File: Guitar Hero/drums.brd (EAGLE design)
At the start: 40.6 x 31.1 mm, 10 parts, among them IC1 ICL7641P

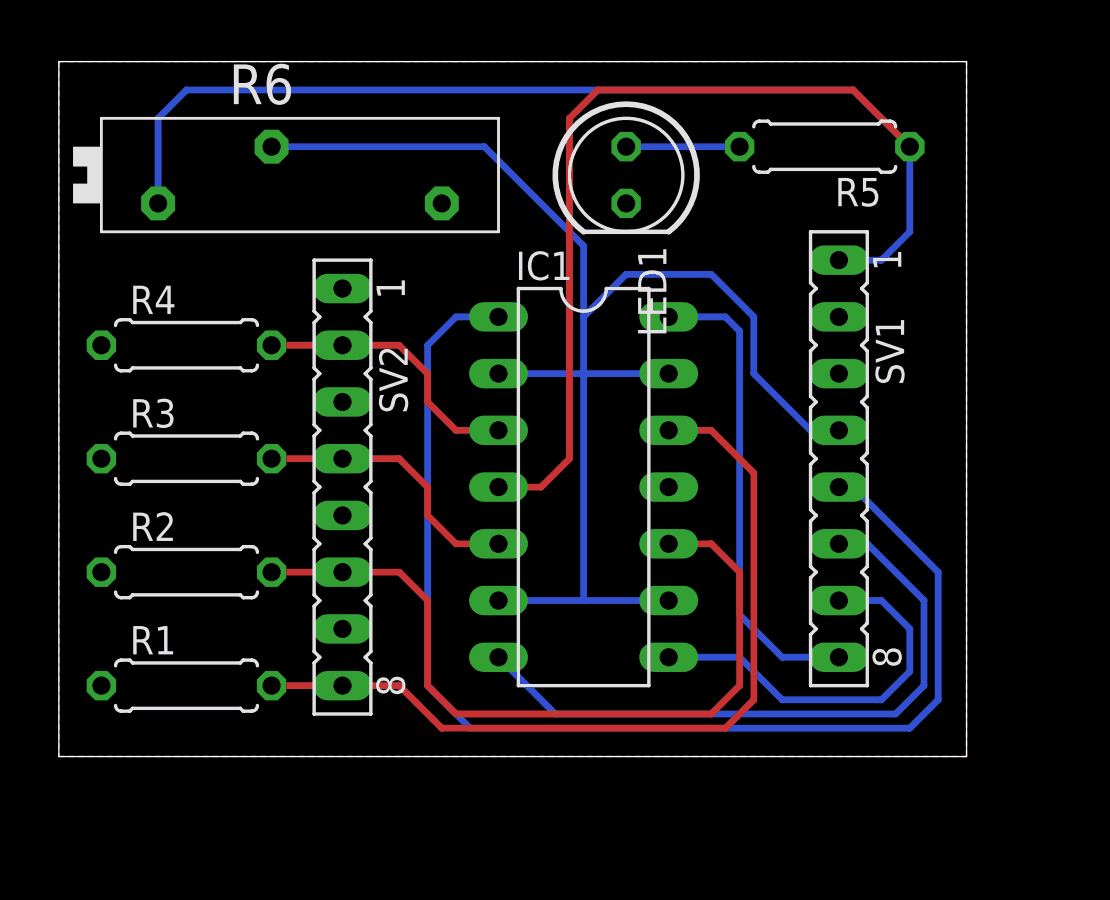
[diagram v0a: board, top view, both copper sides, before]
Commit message: Widened power traces
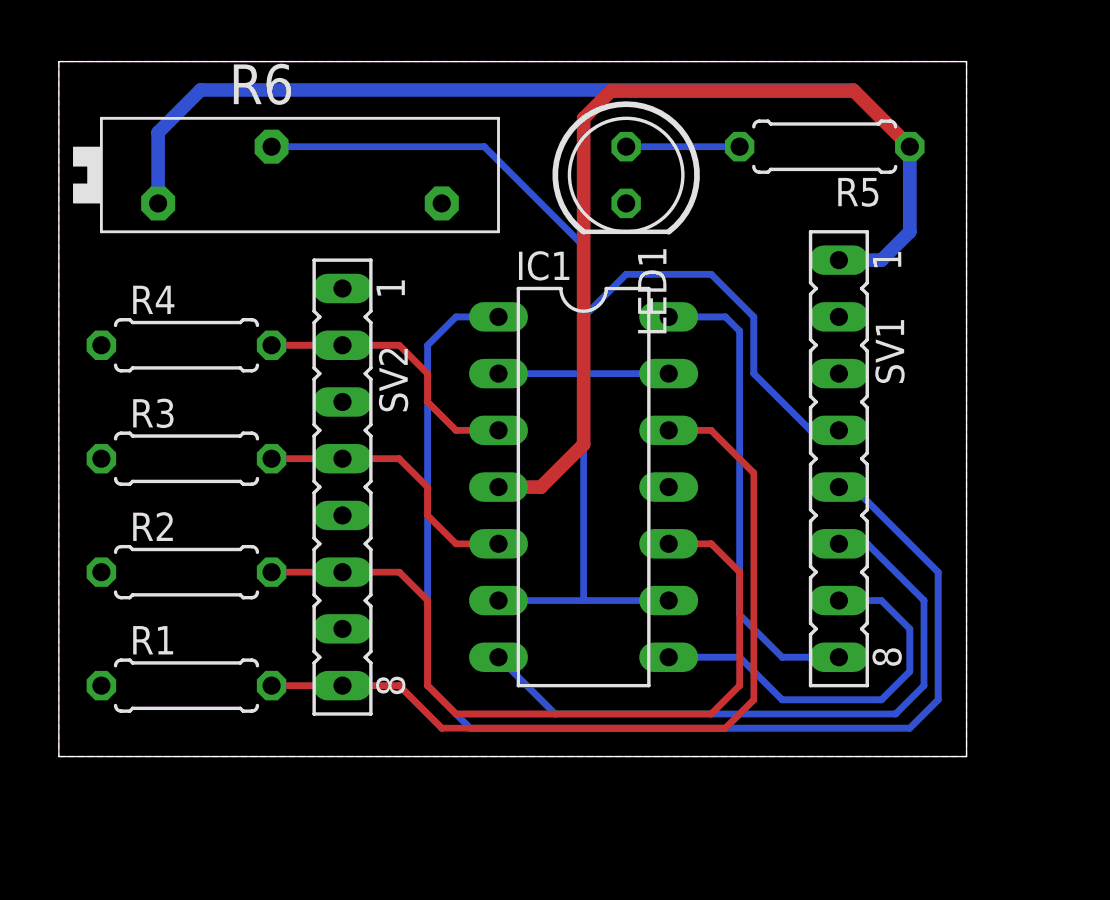
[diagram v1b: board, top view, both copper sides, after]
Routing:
- net VCC: track 82.3 -> 81.5 mm
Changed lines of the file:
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@@
 <contactref element="IC1" pad="4"/>
 <contactref element="R6" pad="1"/>
-<wire x1="48.26" y1="45.72" x2="50.165" y2="45.72" width="0.3048" layer="16"/>
-<wire x1="50.165" y1="45.72" x2="51.435" y2="46.99" width="0.3048" layer="16"/>
-<wire x1="51.435" y1="50.8" x2="51.435" y2="46.99" width="0.3048" layer="16"/>
-<wire x1="17.78" y1="48.26" x2="17.78" y2="52.07" width="0.3048" layer="16"/>
-<wire x1="17.78" y1="52.07" x2="19.05" y2="53.34" width="0.3048" layer="16"/>
-<wire x1="19.05" y1="53.34" x2="48.895" y2="53.34" width="0.3048" layer="16"/>
-<wire x1="48.895" y1="53.34" x2="51.435" y2="50.8" width="0.3048" layer="16"/>
-<wire x1="33.02" y1="35.56" x2="34.925" y2="35.56" width="0.3048" layer="1"/>
-<wire x1="34.925" y1="35.56" x2="36.195" y2="36.83" width="0.3048" layer="1"/>
-<wire x1="36.195" y1="36.83" x2="36.195" y2="52.07" width="0.3048" layer="1"/>
-<wire x1="36.195" y1="52.07" x2="37.465" y2="53.34" width="0.3048" layer="1"/>
-<wire x1="37.465" y1="53.34" x2="48.895" y2="53.34" width="0.3048" layer="1"/>
-<wire x1="48.895" y1="53.34" x2="51.435" y2="50.8" width="0.3048" layer="1"/>
+<wire x1="51.435" y1="50.8" x2="48.9458" y2="53.2892" width="0.6096" layer="1"/>
+<wire x1="48.9458" y1="53.2892" x2="38.0492" y2="53.2892" width="0.6096" layer="1"/>
+<wire x1="38.0492" y1="53.2892" x2="36.83" y2="52.07" width="0.6096" layer="1"/>
+<wire x1="36.83" y1="52.07" x2="36.83" y2="37.465" width="0.6096" layer="1"/>
+<wire x1="36.83" y1="37.465" x2="34.925" y2="35.56" width="0.6096" layer="1"/>
+<wire x1="34.925" y1="35.56" x2="33.02" y2="35.56" width="0.6096" layer="1"/>
+<wire x1="48.26" y1="45.72" x2="50.165" y2="45.72" width="0.6096" layer="16"/>
+<wire x1="50.165" y1="45.72" x2="51.435" y2="46.99" width="0.6096" layer="16"/>
+<wire x1="51.435" y1="46.99" x2="51.435" y2="50.8" width="0.6096" layer="16"/>
+<wire x1="51.435" y1="50.8" x2="48.895" y2="53.34" width="0.6096" layer="16"/>
+<wire x1="48.895" y1="53.34" x2="19.685" y2="53.34" width="0.6096" layer="16"/>
+<wire x1="19.685" y1="53.34" x2="17.78" y2="51.435" width="0.6096" layer="16"/>
+<wire x1="17.78" y1="51.435" x2="17.78" y2="48.26" width="0.6096" layer="16"/>
 </signal>
 <signal name="N$2">

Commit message: Nano++ schematic; guitar hero redo to not use 1/64th bit
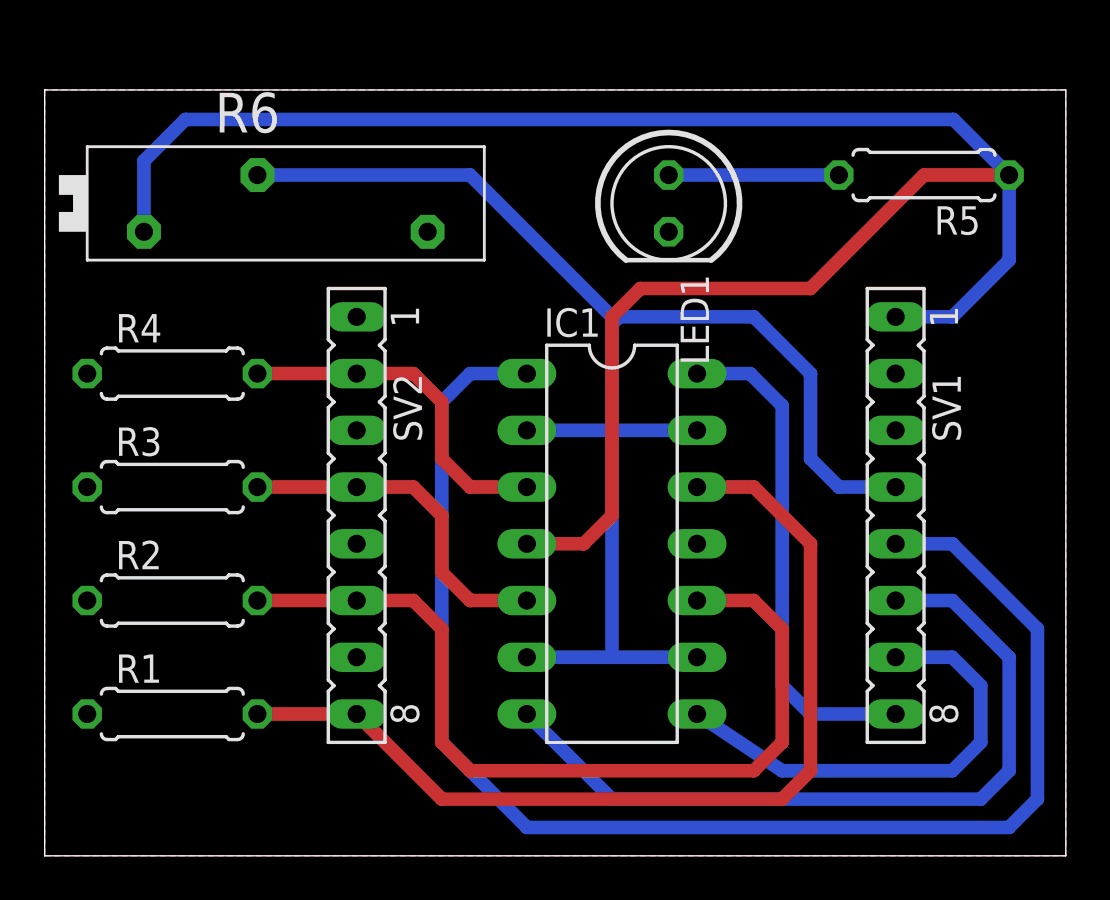
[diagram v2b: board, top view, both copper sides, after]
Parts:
- moved R5 4.62 mm to (52.1, 49.5)
- moved SV1 3.59 mm to (50.8, 34.3)
- moved IC1 2.84 mm to (38.1, 33.0)
- moved LED1 2.29 mm to (40.6, 48.3)
- moved R1 1.42 mm to (18.4, 25.4)
- moved SV2 1.42 mm to (26.7, 34.3)
- moved R6 1.42 mm to (23.5, 48.3)
- moved R2 1.42 mm to (18.4, 30.5)
- moved R3 1.42 mm to (18.4, 35.6)
- moved R4 1.42 mm to (18.4, 40.6)
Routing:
- net B1: track 54.9 -> 63.9 mm
- net VCC: track 81.5 -> 87.3 mm
- net B2: track 29.3 -> 34.9 mm
- net D4: track 37.7 -> 43.2 mm
- net D3: track 35.1 -> 39.6 mm
- net VREF: track 63.6 -> 67.2 mm
- net D2: track 12.5 -> 15.7 mm
- net D1: track 12.5 -> 15.7 mm
- net B3: track 17.7 -> 20.9 mm
- net N$2: track 5.08 -> 7.62 mm
- net B4: track 21.4 -> 22.5 mm
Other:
- board size 40.6 x 31.1 mm -> 45.7 x 34.3 mm
